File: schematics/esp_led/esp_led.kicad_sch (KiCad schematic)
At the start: 10 parts, among them J1 ESP32-WROOM-DevKit, SW1 Color_Switch

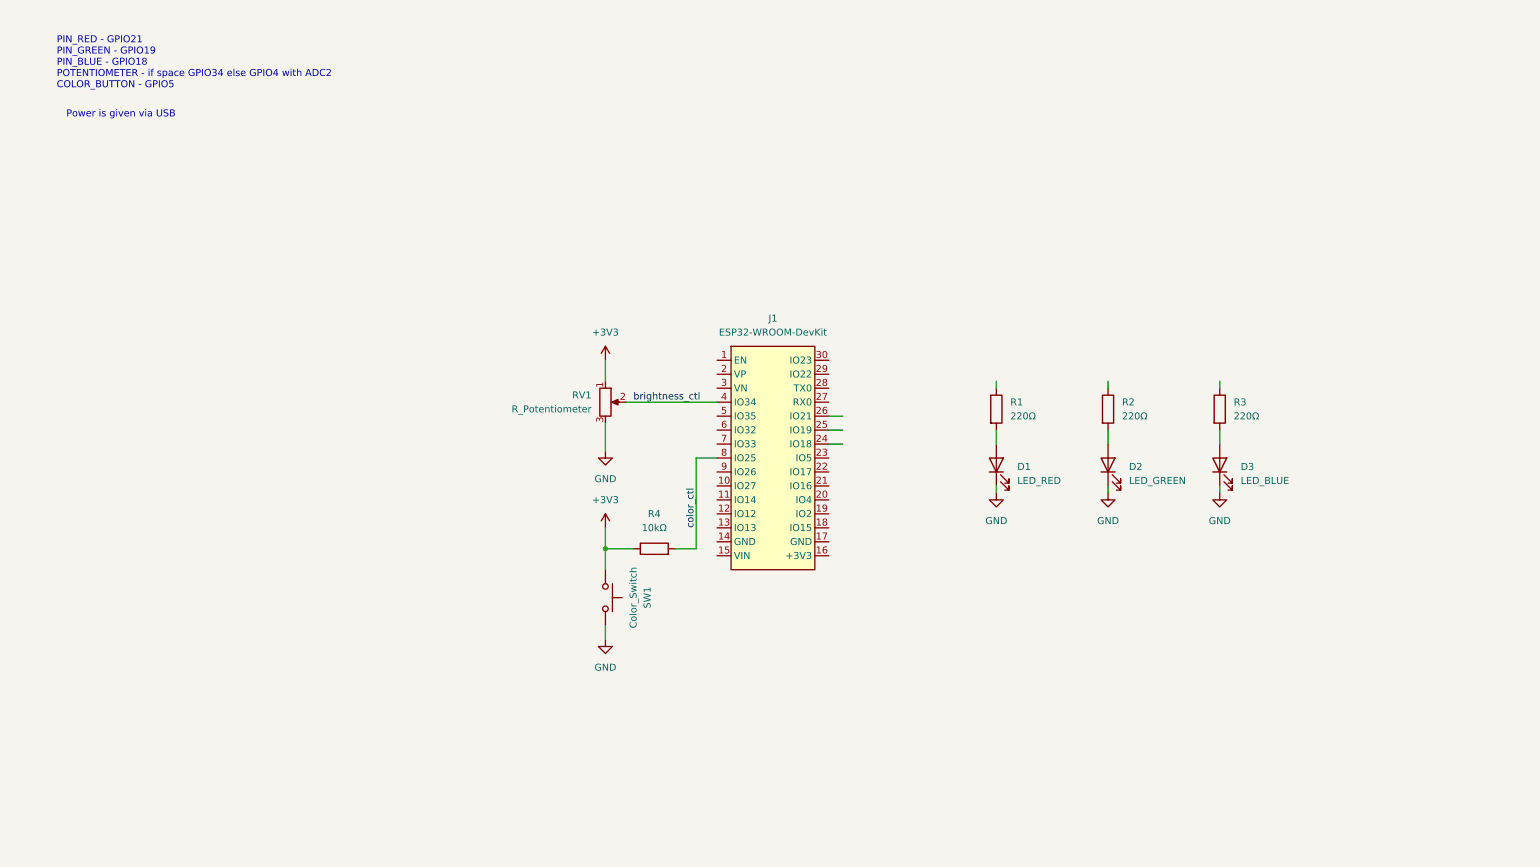
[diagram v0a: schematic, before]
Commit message: Adding sleep after 60 seconds of downtime and separating the functions and declarations out of main. Also adding MosFETs to the schematic without connecting
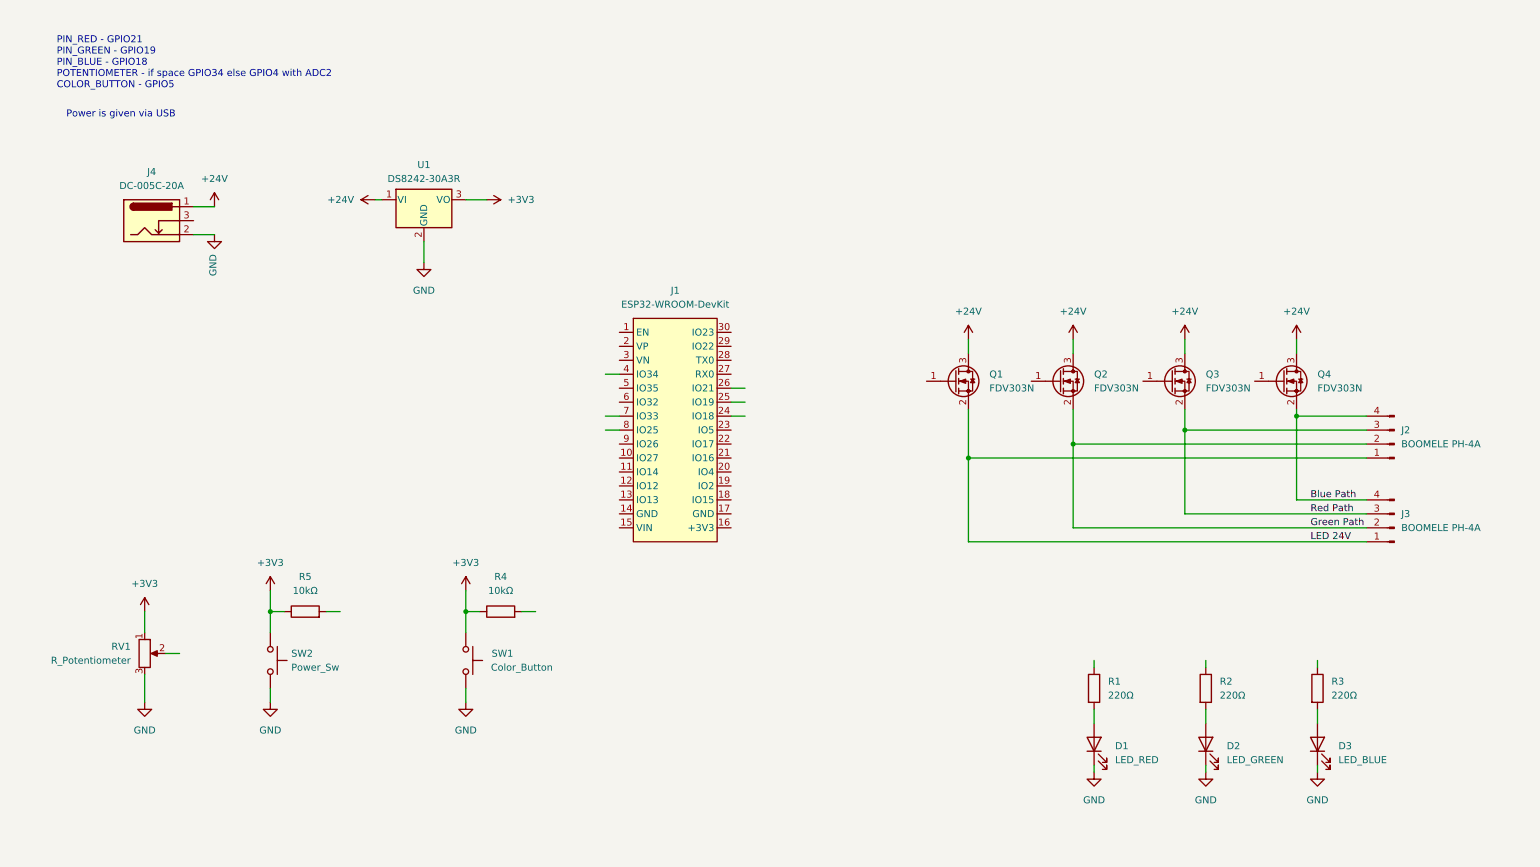
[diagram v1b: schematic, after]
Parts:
- added J2, J3: BOOMELE PH-4A, Connector_Molex:Molex_MicroClasp_55932-0430_1x04_P2.00mm_Vertical, symbol Connector:Conn_01x04_Pin
- added J4: DC-005C-20A, Connector_BarrelJack:BarrelJack_Horizontal, symbol Connector:Barrel_Jack_Switch
- added Q1, Q2, Q3, Q4: FDV303N, Package_TO_SOT_SMD:SOT-23, symbol Transistor_FET:DMG2302U
- added R5: 10kΩ, symbol Device:R
- added SW2: Power_Sw, symbol Switch:SW_Push
- added U1: DS8242-30A3R, Package_TO_SOT_SMD:TO-252-2, symbol Regulator_Linear:KF33BDT
- SW1: value Color_Switch -> Color_Button
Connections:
- net +3V3: now also R5.1, SW2.1, U1.3 (VO)
- net GND: now also J4.2, SW2.2, U1.2 (GND)
- net brightness_ctl: no longer names the net of RV1.2
- net brightness_ctl: no longer J1.4 (IO34)
- net color_ctl: no longer names the net of R4.2
- net color_ctl: no longer J1.8 (IO25)
- new net +24V: J4.1, Q1.3 (D), Q2.3 (D), Q3.3 (D), Q4.3 (D), U1.1 (VI)
- new net Blue Path: J2.4 (Pin_4), J3.4 (Pin_4), Q4.2 (S)
- new net Green Path: J2.2 (Pin_2), J3.2 (Pin_2), Q2.2 (S)
- new net LED 24V: J2.1 (Pin_1), J3.1 (Pin_1), Q1.2 (S)
- new net Red Path: J2.3 (Pin_3), J3.3 (Pin_3), Q3.2 (S)
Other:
- moved on the sheet: D1, D2, D3, J1, R1, R2, R3, R4, RV1, SW1

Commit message: I implemented basic mqtt handling and wifi initialization. I also added a few things to the electrical schematic.
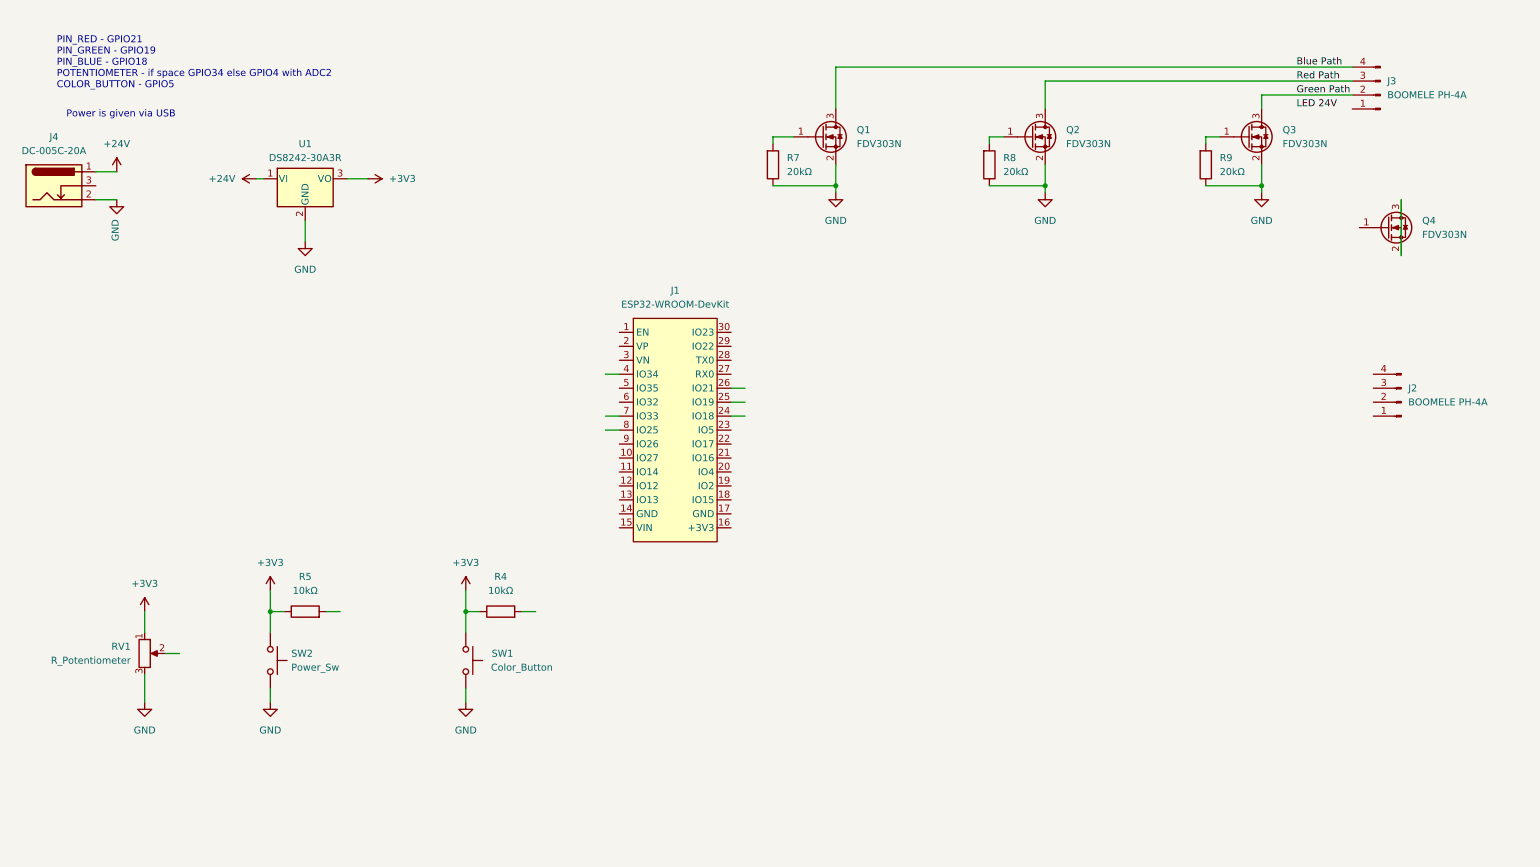
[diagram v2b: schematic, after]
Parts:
- removed D1: LED_RED, symbol Device:LED
- removed D2: LED_GREEN, symbol Device:LED
- removed D3: LED_BLUE, symbol Device:LED
- removed R1, R2, R3: 220Ω, symbol Device:R
- added R7, R8, R9: 20kΩ, Resistor_SMD:R_0201_0603Metric, symbol Resistor:0603WAF2002T5E
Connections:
- net +24V: no longer Q1.3 (D), Q2.3 (D), Q3.3 (D), Q4.3 (D)
- net Blue Path: now also Q1.3 (D); no longer J2.4 (Pin_4), Q4.2 (S)
- net GND: now also Q1.2 (S), Q2.2 (S), Q3.2 (S), R7.2, R8.2, R9.2
- net Green Path: now also Q3.3 (D); no longer J2.2 (Pin_2), Q2.2 (S)
- net LED 24V: no longer J2.1 (Pin_1), J3.1 (Pin_1), Q1.2 (S)
- net Red Path: now also Q2.3 (D); no longer J2.3 (Pin_3), Q3.2 (S)
- net at Q2.1 (G): now also R8.1
- net at Q3.1 (G): now also R9.1
- net at Q1.1 (G): now also R7.1
- new net: Q4.2 (S), Q4.3 (D)
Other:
- moved on the sheet: J2, J3, J4, Q1, Q2, Q3, Q4, U1

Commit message: I tried my best at implementing the Buck Converter correctly. The Code is not yet ready to allow the new pin usages and two different LED stripes
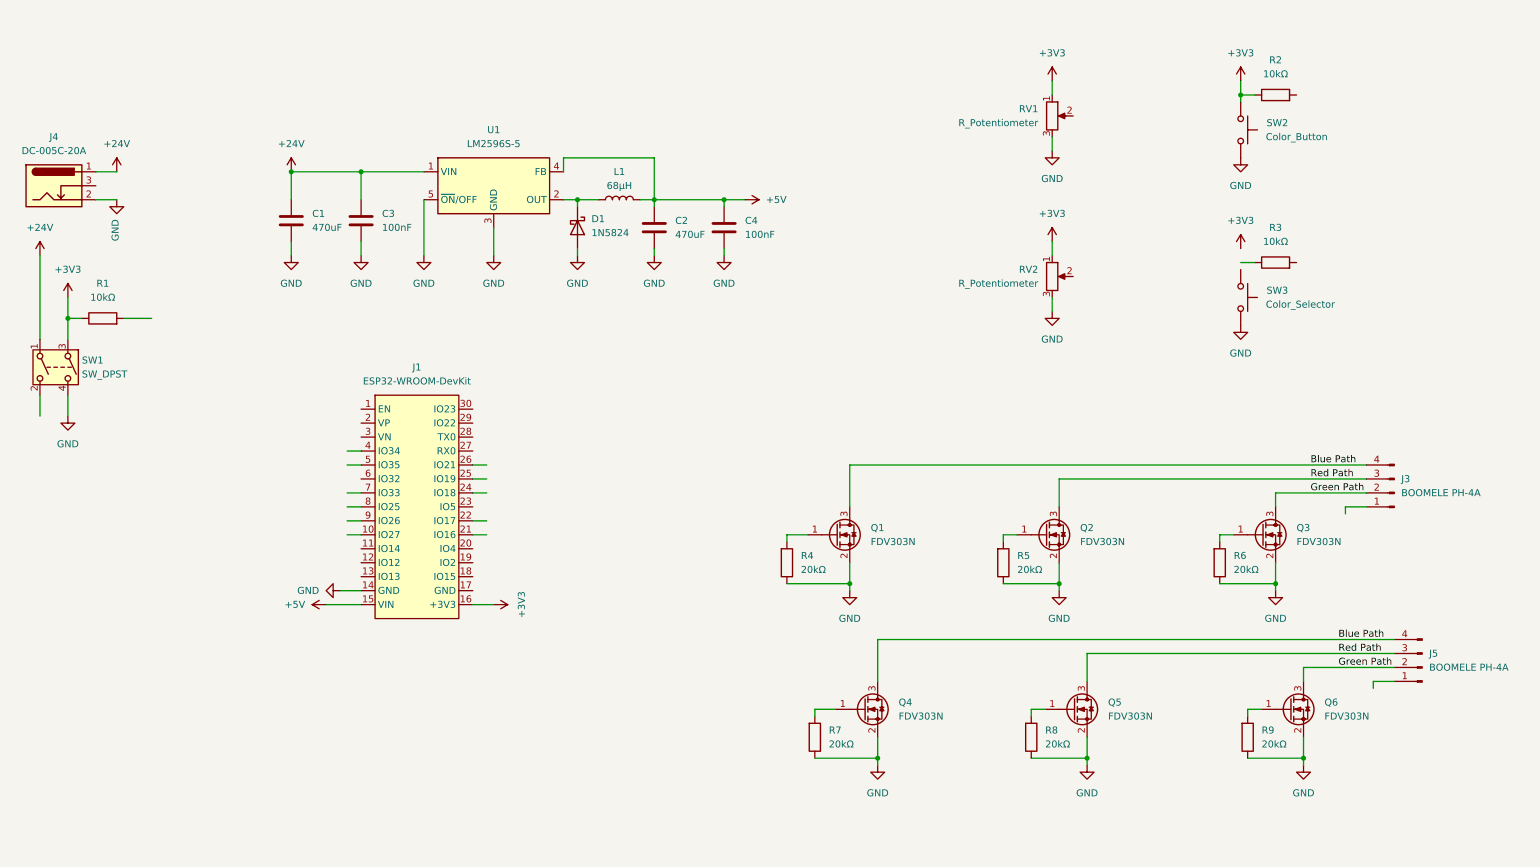
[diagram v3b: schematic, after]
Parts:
- removed J2: BOOMELE PH-4A, Connector_Molex:Molex_MicroClasp_55932-0430_1x04_P2.00mm_Vertical, symbol Connector:Conn_01x04_Pin
- removed SW2: Power_Sw, symbol Switch:SW_Push
- removed U1: DS8242-30A3R, Package_TO_SOT_SMD:TO-252-2, symbol Regulator_Linear:KF33BDT
- added C1, C2: 470uF, Capacitor_THT:C_Radial_D10.0mm_H16.0mm_P5.00mm, symbol Device:C
- added C3, C4: 100nF, Capacitor_SMD:C_0201_0603Metric, symbol Device:C
- added D1: 1N5824, Diode_THT:D_DO-201AD_P15.24mm_Horizontal, symbol Device:D_Schottky
- added J5: BOOMELE PH-4A, Connector_Molex:Molex_MicroClasp_55932-0430_1x04_P2.00mm_Vertical, symbol Connector:Conn_01x04_Pin
- added L1: 68μH, Inductor_SMD:L_Sunlord_MWSA1005S, symbol Device:L
- added Q5, Q6: FDV303N, Package_TO_SOT_SMD:SOT-23, symbol Transistor_FET:DMG2302U
- added R3: 10kΩ, symbol Device:R
- added R7, R8, R9: 20kΩ, Resistor_SMD:R_0201_0603Metric, symbol Resistor:0603WAF2002T5E
- added RV2: R_Potentiometer, symbol Device:R_Potentiometer
- added SW1: SW_DPST, symbol Switch:SW_DPST
- added SW3: Color_Selector, symbol Switch:SW_Push
- added U1: LM2596S-5, Package_TO_SOT_SMD:TO-263-5_TabPin3, symbol Regulator_Switching:LM2596S-5
- renumbered R5 to R1, R4 to R2, R7 to R4, R8 to R5, R9 to R6, SW1 to SW2
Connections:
- net +24V: now also C1.1, C3.1, SW1.1, U1.1 (VIN)
- net +3V3: now also J1.16 (+3V3), RV2.1, SW1.3
- net Blue Path: now also Q4.3 (D), J5.4 (Pin_4)
- net GND: now also J1.14 (GND), Q4.2 (S), C1.2, C2.2, C3.2, C4.2, D1.2 (A), Q5.2 (S), Q6.2 (S), R7.2, R8.2, R9.2, RV2.3, SW1.4, SW3.2, U1.3 (GND), U1.5 (~{ON}/OFF)
- net Green Path: now also J5.2 (Pin_2), Q6.3 (D)
- net Red Path: now also J5.3 (Pin_3), Q5.3 (D)
- net at Q4.1 (G): now also R7.1
- net +5V: now reaches J1.15 (VIN)
- net +5V: now also C2.1, C4.1, L1.2, U1.4 (FB)
- new net: Q5.1 (G), R8.1
- new net: D1.1 (K), L1.1, U1.2 (OUT)
- new net: Q6.1 (G), R9.1
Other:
- note removed: "PIN_RED - GPIO21 PIN_GREEN - GPIO19 PIN_BLUE - GPIO18 POTENTIOMETER - if space GPIO34 else GPIO4 with ADC2 COLOR_BUTTON - GPIO5"
- note removed: "Power is given via USB"
- title: (none) -> ESP32 LED
- moved on the sheet: J1, J3, Q1, Q2, Q3, R1, R2, R4, R5, R6, RV1, SW2

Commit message: The code now also supports two different LED stripes; with the addition of a main switch for turning of the lights and a selector switch to choose which of the two LED stripes to change. In addition it appears as two distinct lights in home assistant.
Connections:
- net +3V3: now also R3.1, SW3.1
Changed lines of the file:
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@@
+	)
+	(junction
+		(at 240.03 62.23)
+		(diameter 0)
+		(color 0 0 0 0)
 	)
 	(junction
@@
 	(wire
 		(pts
+			(xy 240.03 59.69) (xy 240.03 62.23)
+		)
+		(stroke
+			(width 0)
+			(type default)
+		)
+	)
+	(wire
+		(pts
 			(xy 168.91 99.06) (xy 168.91 106.68)
 		)
@@
 		(pts
 			(xy 31.75 50.8) (xy 35.56 50.8)
+		)
+		(stroke
+			(width 0)
+			(type default)
+		)
+	)
+	(wire
+		(pts
+			(xy 240.03 62.23) (xy 240.03 63.5)
 		)
 		(stroke
@@
 			(justify right bottom)
 		)
-		(property "Netclass" "Color_Btn_1"
-			(at 118.11 109.22 0)
-			(effects
-				(font
+		(property "Netclass" "Color_Btn"
+			(at 116.078 109.22 0)
+			(effects
+				(font
